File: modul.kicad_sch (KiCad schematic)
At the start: 39 parts, among them Q1 BC848, Q2 BC848, Q3 BC848, U20 TDA8501, X3 4.433618MHz

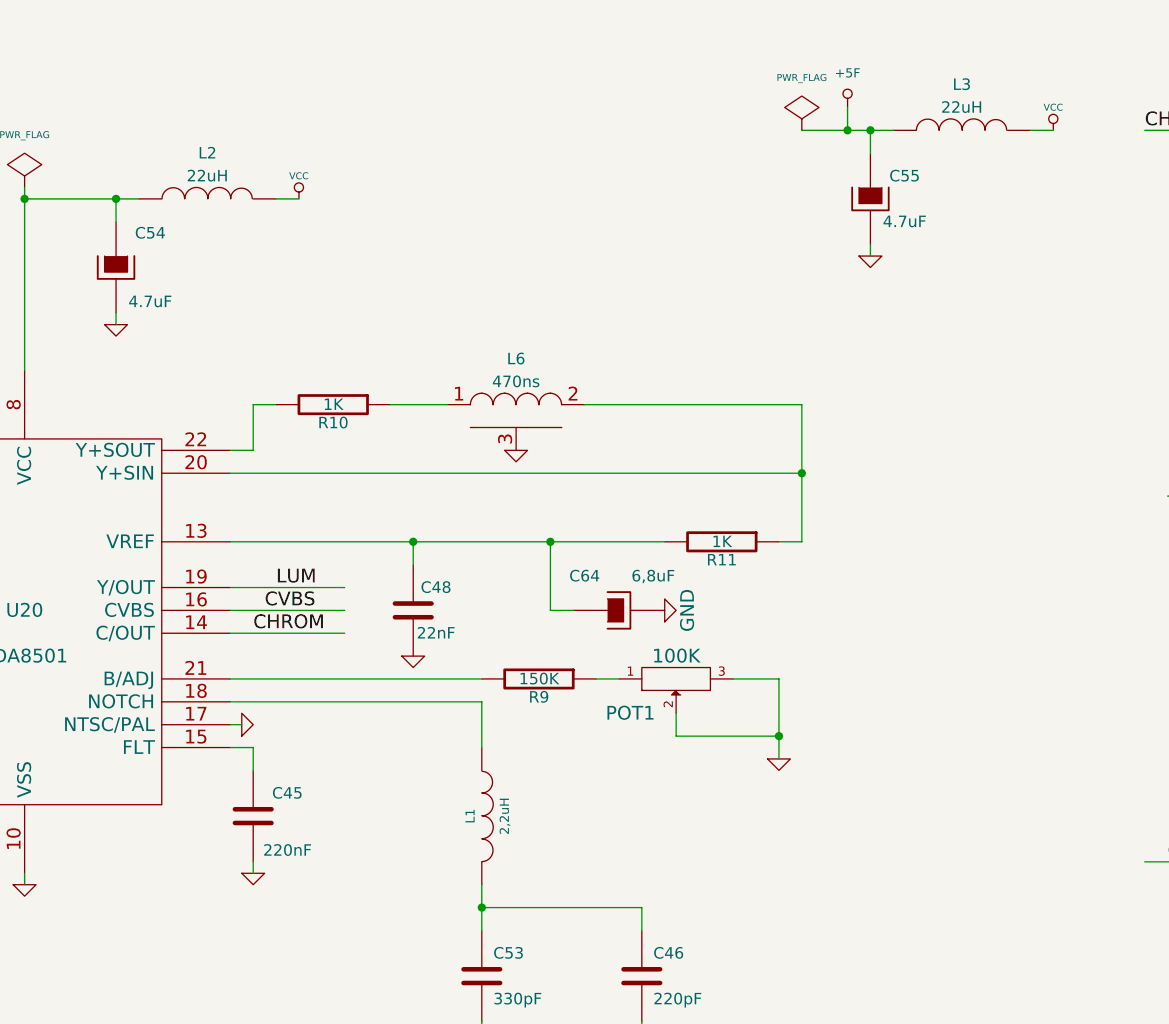
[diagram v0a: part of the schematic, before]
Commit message: update to kicad 9
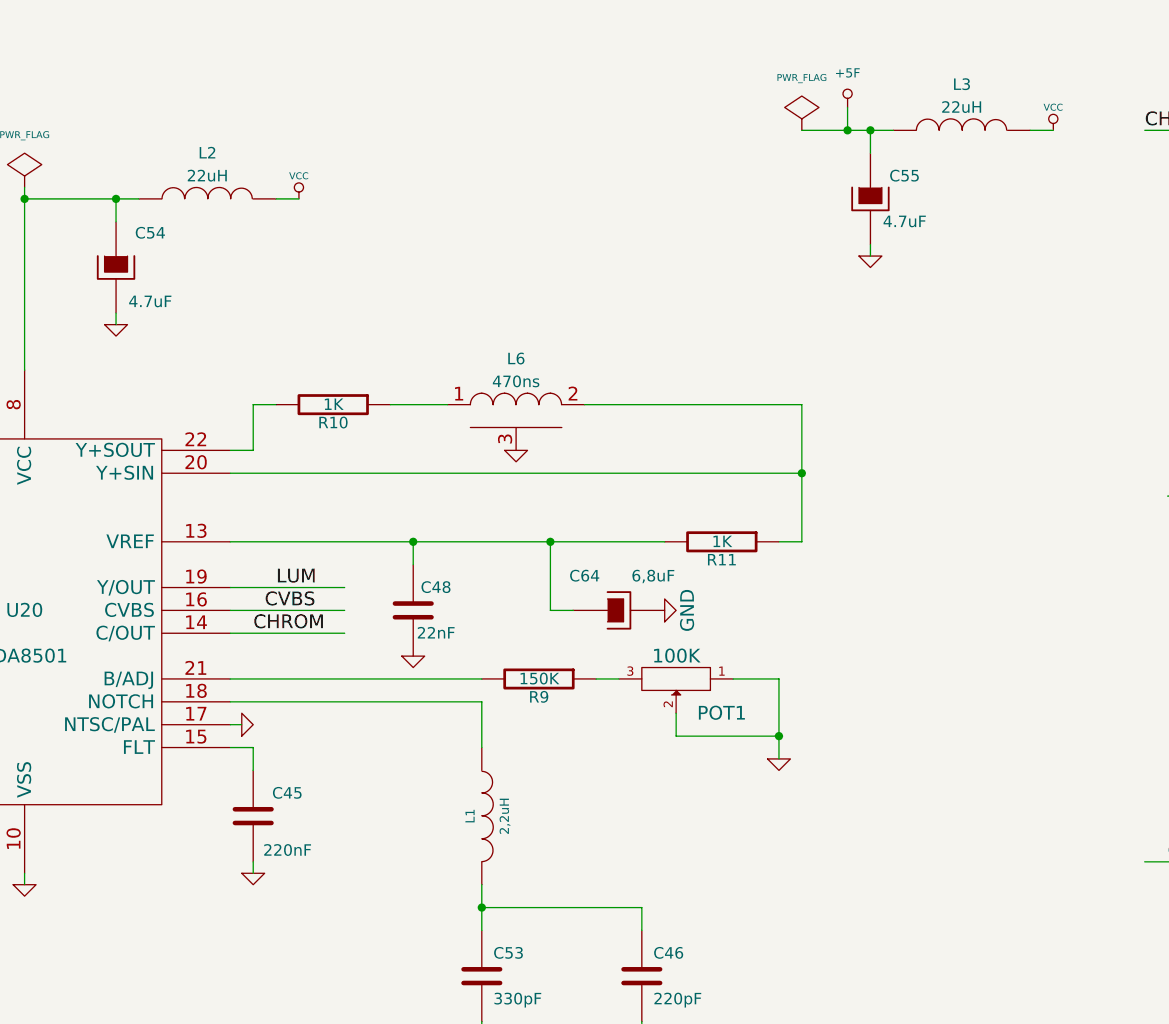
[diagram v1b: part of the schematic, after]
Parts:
- C43, C44, C45, C46, C48, C53, C54, C58, C59, C60, C61, R10, R11, R16, R17, R18, R30, R31, R32, R33, R34, R39, R4, R40, R41, R9: footprint Resistor_SMD:R_1206_3216Metric_Pad1.24x1.80mm_HandSolder -> Resistor_SMD:R_1206_3216Metric_Pad1.30x1.75mm_HandSolder
- C55, C64: footprint Resistor_SMD:R_1210_3225Metric_Pad1.24x2.70mm_HandSolder -> Resistor_SMD:R_1210_3225Metric_Pad1.30x2.65mm_HandSolder
- CV1: footprint Discret:CV3-30PF -> footprints:CV3-30PF
- L1, L2, L3: footprint Resistor_SMD:R_1812_4532Metric_Pad1.24x3.50mm_HandSolder -> Resistor_SMD:R_1812_4532Metric_Pad1.30x3.40mm_HandSolder
- POT1: footprint lib_smd:POT_CMS -> Potentiometer_SMD:Potentiometer_Bourns_3314G_Vertical
- Q1, Q2, Q3: footprint lib_smd:SOT23EBC -> footprints:SOT23EBC
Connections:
- net GND: now also POT1.1; no longer POT1.3
- net at R9.1: now also POT1.3; no longer POT1.1
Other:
- moved on the sheet: POT1
